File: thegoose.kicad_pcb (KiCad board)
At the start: 2 copper layers, 73.8 x 52 mm, 42 parts, among them U1 DRV8848, U2 DRV8848, U3 DRV8848, U4 AP64500SP-13

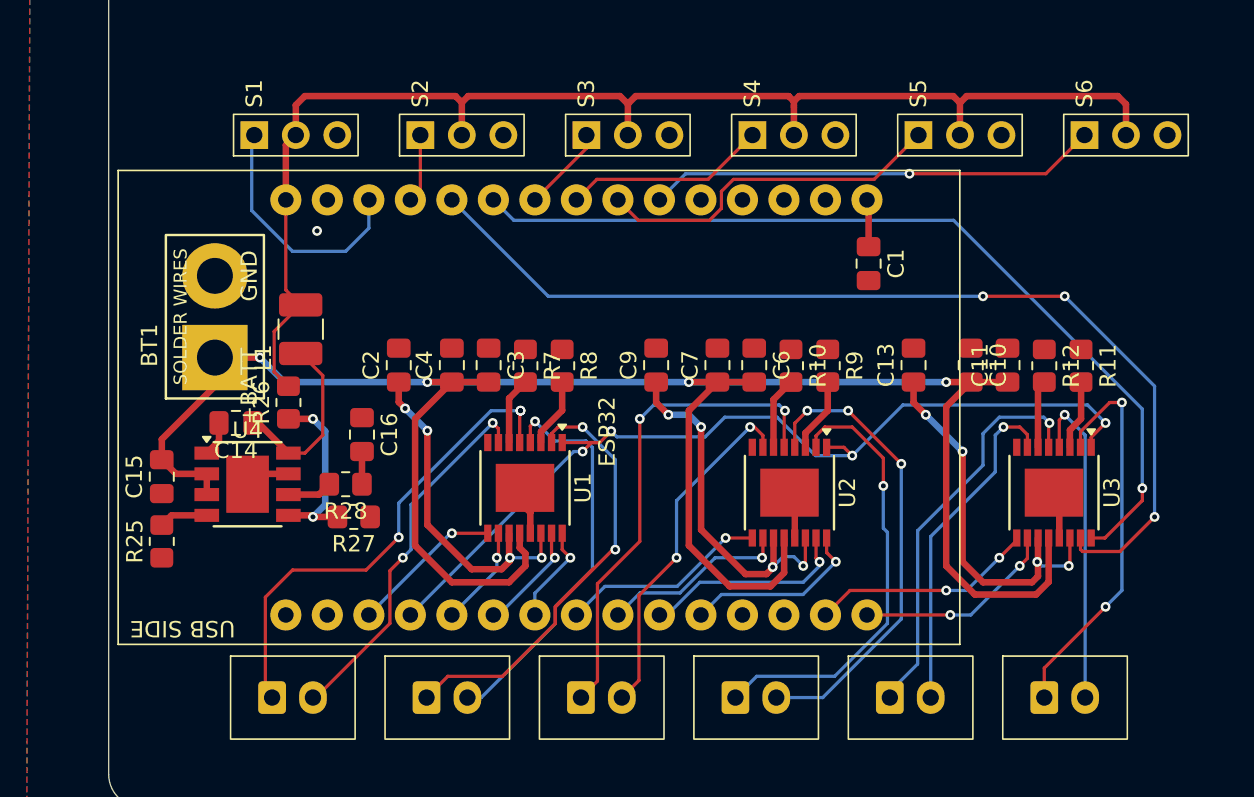
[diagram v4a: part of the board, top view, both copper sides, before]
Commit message: Fix silkscreen
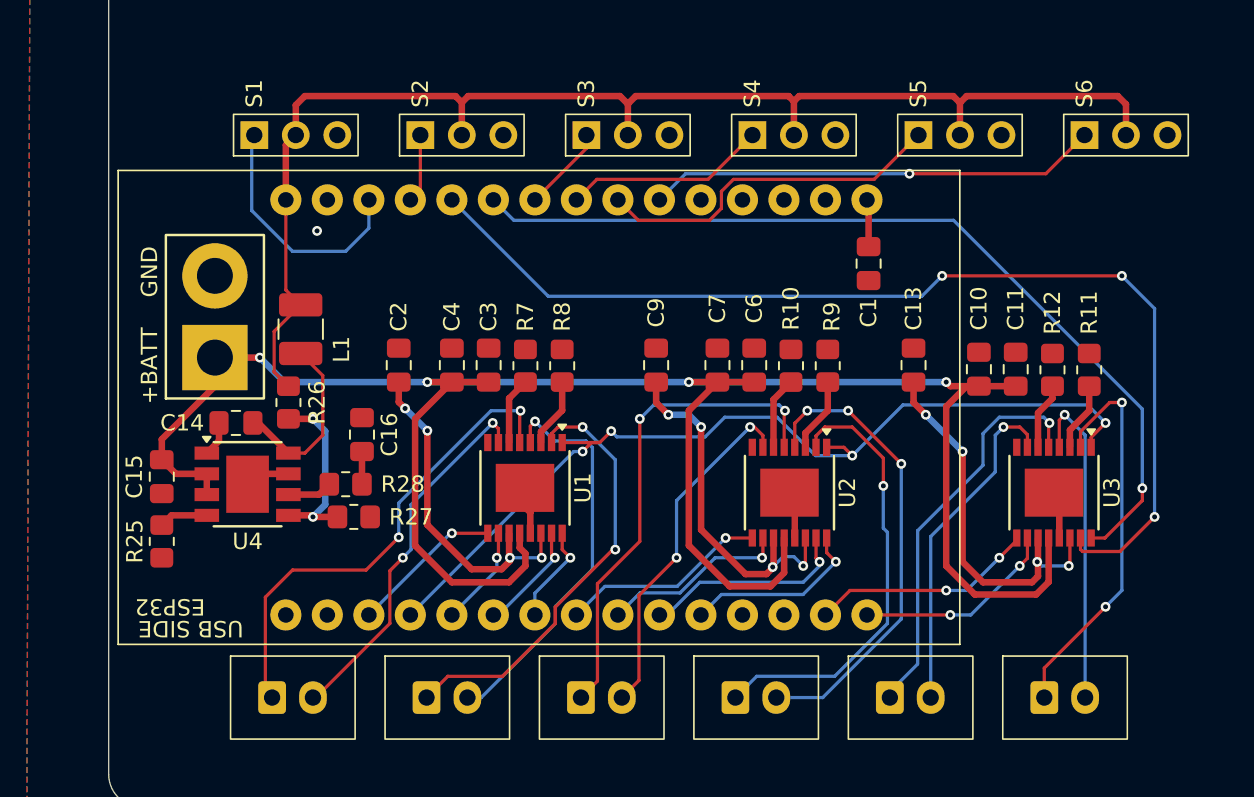
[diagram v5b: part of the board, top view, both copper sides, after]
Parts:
- moved C10 0.56 mm to (171.8, 74.0)
- moved C11 0.56 mm to (174.0, 74.0)
- moved R11 0.56 mm to (178.5, 74.0)
- moved R12 0.56 mm to (176.2, 74.0)
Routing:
- net /ESP_D14: track 61.9 -> 65.7 mm
- net Net-(M2-OUT1): track 31.1 -> 27.9 mm
- net +BATT: track 130.2 -> 131.2 mm
- net Net-(M1-OUT1): track 30.0 -> 29.9 mm, vias 3 -> 2
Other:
- board text added: "+BATT"
- board text added: "GND"

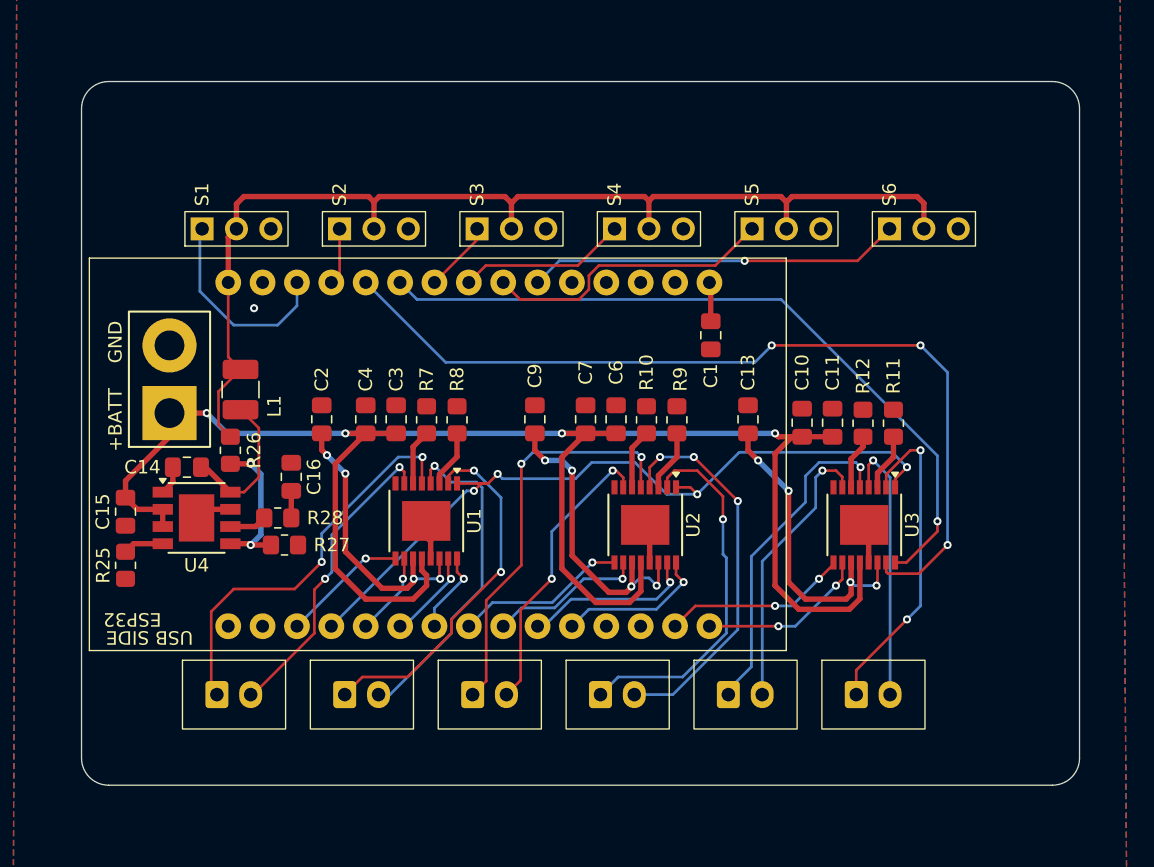
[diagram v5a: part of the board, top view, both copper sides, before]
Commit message: Add mounting holes
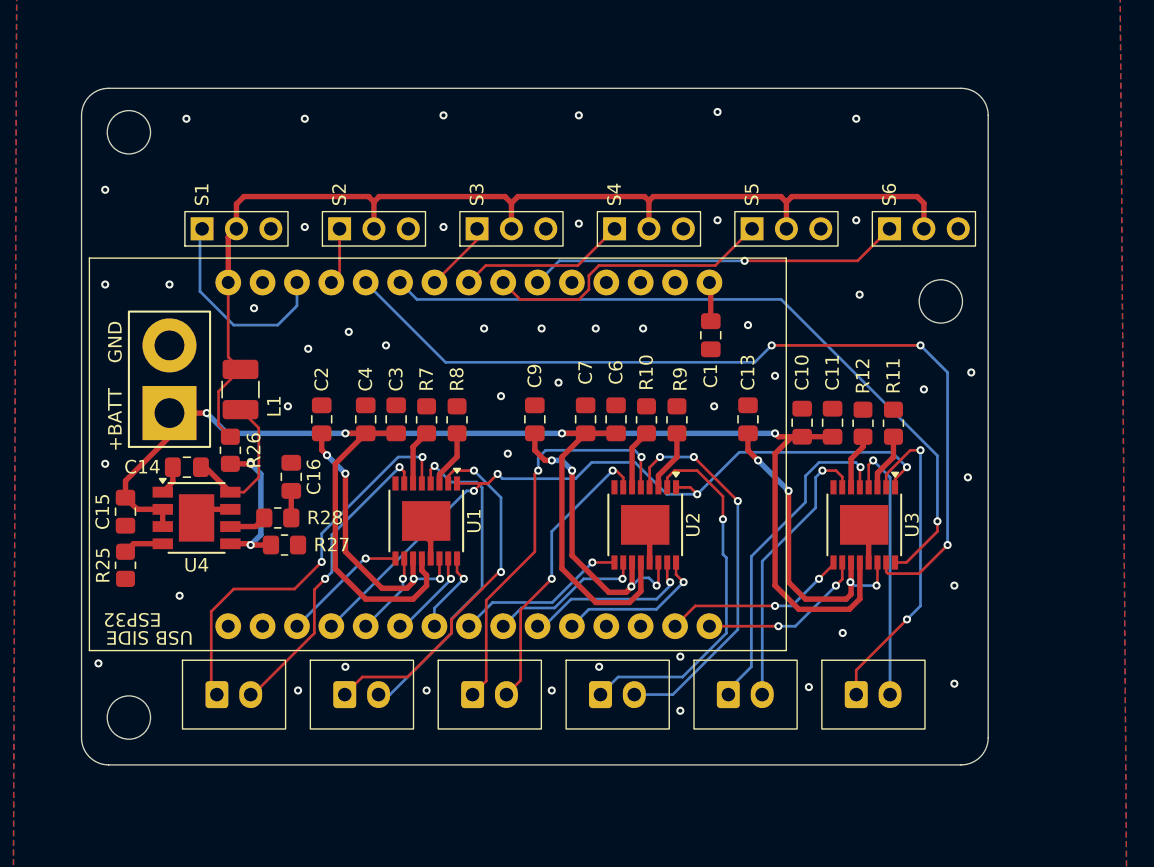
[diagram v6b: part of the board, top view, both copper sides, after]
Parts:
- added REF**: MountingHole_3.2mm_M3, MountingHole:MountingHole_3.2mm_M3, F.Cu at (182.0, 65.0)
- added REF**: MountingHole_3.2mm_M3, MountingHole:MountingHole_3.2mm_M3, F.Cu at (122.0, 95.8)
- added REF**: MountingHole_3.2mm_M3, MountingHole:MountingHole_3.2mm_M3, F.Cu at (122.0, 52.5)
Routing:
- net GND: vias 1 -> 47
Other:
- board size 73.8 x 52 mm -> 67 x 50 mm
